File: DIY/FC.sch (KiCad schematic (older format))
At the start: 6 parts, among them J1 DB15_Female, J2 DB25_Male, U1 74AHCT125N, U2 74AHCT125N, U3 74AHCT125N, U4 74AHCT125N

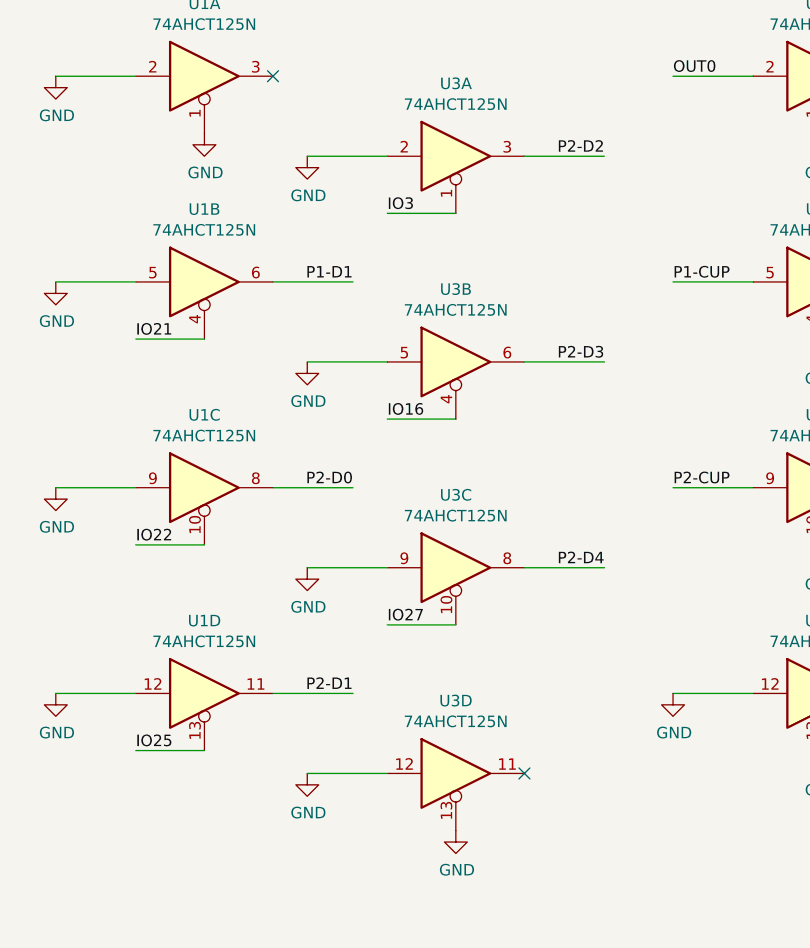
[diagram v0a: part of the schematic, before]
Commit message: Add pullup to OD outputs on ESP side
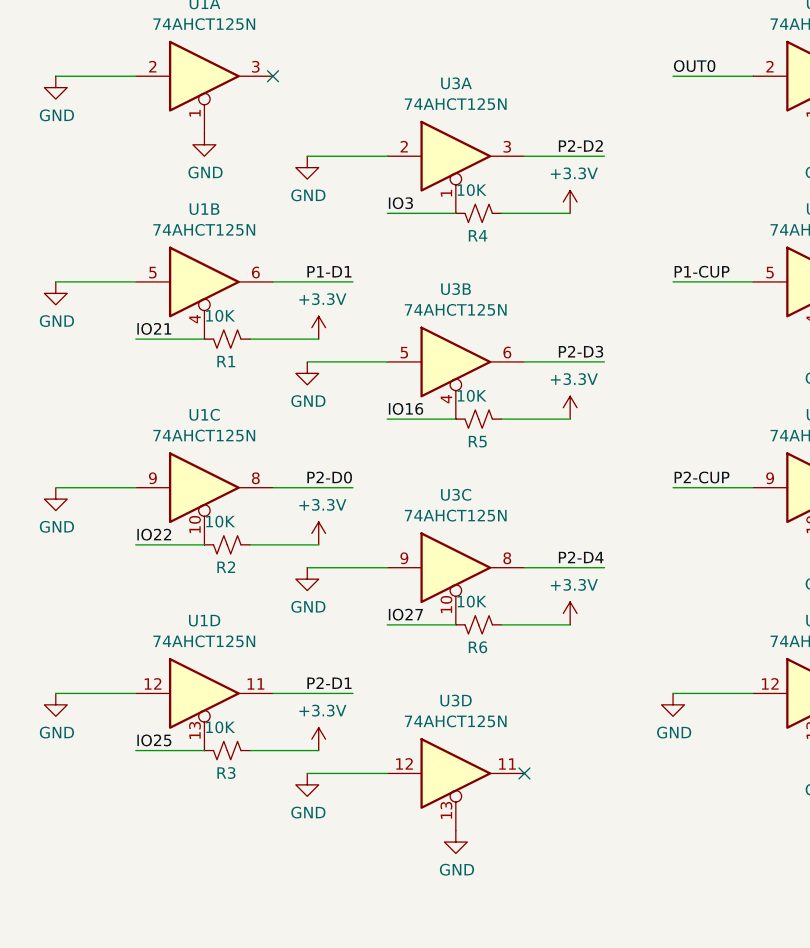
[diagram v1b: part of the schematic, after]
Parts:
- added R1, R2, R3, R4, R5, R6: 10K, symbol Device:R_Small_US
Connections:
- net +3V3: now also R1.1, R2.1, R3.1, R4.1, R5.1, R6.1
- net IO16: now also R5.2
- net IO21: now also R1.2
- net IO22: now also R2.2
- net IO25: now also R3.2
- net IO27: now also R6.2
- net IO3: now also R4.2
